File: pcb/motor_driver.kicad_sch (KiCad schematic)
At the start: 10 parts, among them U4 VNH7070BASTR

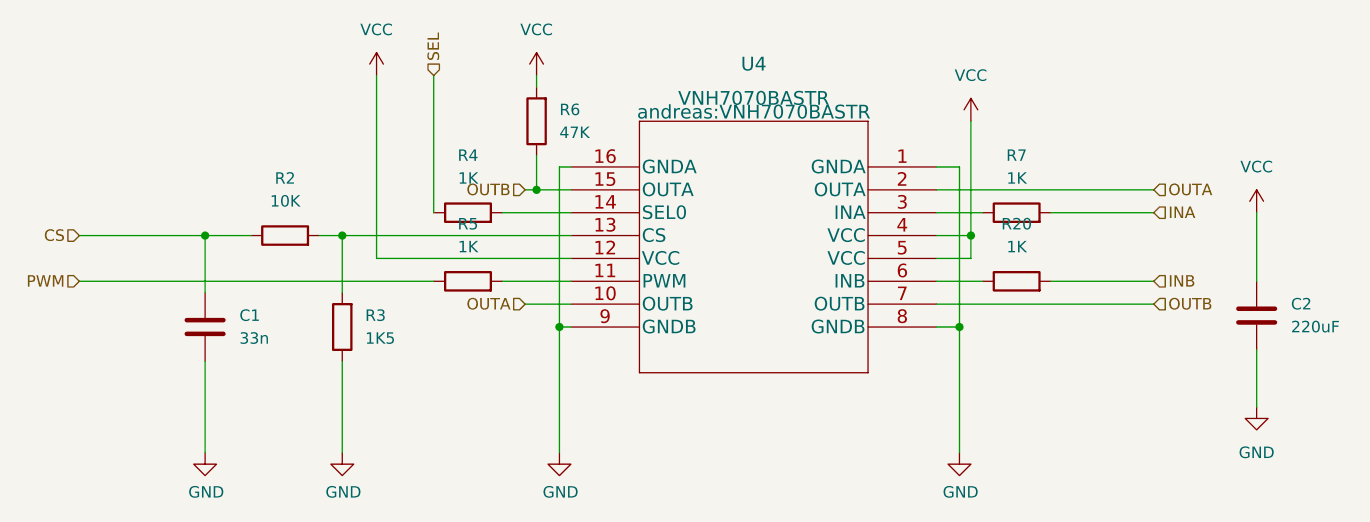
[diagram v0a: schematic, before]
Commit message: Fix some ERC warnings
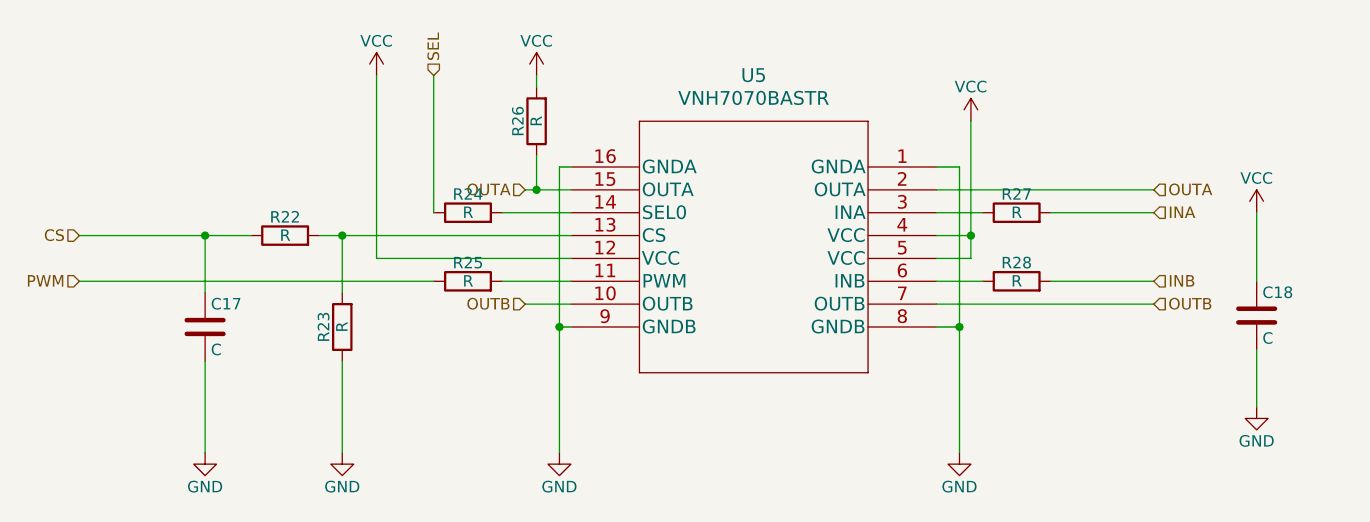
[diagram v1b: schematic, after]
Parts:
- C17: renamed from C1; value 33n -> C
- C18: renamed from C2; value 220uF -> C
- R22: renamed from R2; value 10K -> R
- R23: renamed from R3; value 1K5 -> R
- R24: renamed from R4; value 1K -> R
- R25: renamed from R5; value 1K -> R
- R26: renamed from R6; value 47K -> R
- R27: renamed from R7; value 1K -> R
- R28: renamed from R20; value 1K -> R
- U5: renamed from U4; footprint andreas:VNH7070BASTR -> SO-16N_STM
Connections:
- net OUTA: now also R26.1, U5.15 (OUTA); no longer U5.10 (OUTB)
- net OUTB: now also U5.10 (OUTB); no longer R26.1, U5.15 (OUTA)
